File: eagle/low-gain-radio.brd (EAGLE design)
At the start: 99 x 100 mm, 109 parts, among them Y1 32MHz

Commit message: Added to-do lists
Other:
- board text added: "TODO: -Add PSAS and people who helped with board text -Figure out footprint drc error -I'm guessing we are ignoring the dimension drc error on the MCX???"
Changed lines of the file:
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@@
 <layer number="98" name="Guide" color="6" fill="1" visible="no" active="no"/>
 <layer number="99" name="SpiceOrder" color="7" fill="1" visible="no" active="no"/>
-<layer number="100" name="TODO" color="12" fill="1" visible="no" active="yes"/>
+<layer number="100" name="TODO" color="12" fill="1" visible="yes" active="yes"/>
 <layer number="101" name="Hidden" color="7" fill="1" visible="no" active="yes"/>
 <layer number="102" name="Changes" color="7" fill="1" visible="no" active="yes"/>
@@
 <text x="55.2" y="53.05" size="1" layer="21" font="vector" ratio="16" rot="R180">DIO4</text>
 <text x="45.05" y="86.5" size="1" layer="21" font="vector" ratio="16">PG</text>
+<text x="65.45" y="30.4" size="0.4064" layer="100">TODO:
+-Add PSAS and people who helped with board text
+-Figure out footprint drc error
+-I'm guessing we are ignoring the dimension drc error on the MCX???</text>
 </plain>
 <attributes>

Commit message: Pushing for Andrew
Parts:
- CF2: value CON-MCX-LINX -> CON-MCX-F-LINX-CONMCX003.062
- moved CF2 2.86 mm to (72.0, 93.0)
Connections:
- removed net ASD: C47.1
- net RF_GND: now also C47.1, CF2.SHIELD1, CF2.SHIELD2, CF2.SHIELD3, CF2.SHIELD4
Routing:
- net N$30: track 3.79 -> 9.46 mm
- net RF_GND: track 11.8 -> 13.7 mm
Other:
- outline, holes or cut-outs redrawn
- board text added: "TODO: -Add PSAS and people who helped with board text -Via stitching"
- board text removed: "Cut power plane to here"
- board text removed: "TODO: -Add PSAS and people who helped with board text -Figure out footprint drc error -I'm guessing we are ignoring the dimension drc error on the MCX???"
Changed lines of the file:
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@@
 <text x="35" y="0.6" size="1" layer="21" font="vector" ratio="16">C2</text>
 <text x="14.2" y="0.6" size="1" layer="21" font="vector" ratio="16">GND</text>
-<wire x1="49.8" y1="89.6" x2="49.85" y2="89.6" width="0.2" layer="100" style="longdash"/>
-<wire x1="49.85" y1="89.6" x2="49.85" y2="71.25" width="0.2" layer="100" style="shortdash"/>
-<wire x1="49.85" y1="71.25" x2="59.75" y2="71.25" width="0.2" layer="100" style="shortdash"/>
-<text x="49.65" y="90.35" size="0.75" layer="100">Cut power plane to here</text>
 <text x="62.15" y="62.8" size="1" layer="21" font="vector" ratio="16">XTA</text>
 <text x="97.45" y="71.6" size="1" layer="21" font="vector" ratio="16" rot="R180">SCLK</text>
@@
 <text x="65.45" y="30.4" size="0.4064" layer="100">TODO:
 -Add PSAS and people who helped with board text
--Figure out footprint drc error
--I'm guessing we are ignoring the dimension drc error on the MCX???</text>
+-Via stitching</text>
 </plain>
 <attributes>
@@
 </element>
 <element name="CF1" library="oresat-eagle" package="HARWIN-ARCHER-M50-3202045" value="ORESAT-CONNECTOR-40PIN" x="30.065" y="95.46" locked="yes" rot="R180"/>
-<element name="CF2" library="oresat-eagle" package="CON-MCX-LINX-CONMCX003.062" value="CON-MCX-LINX" x="72.04" y="90.119" locked="yes" rot="R90"/>
+<element name="CF2" library="oresat-eagle" package="CON-MCX-LINX-CONMCX003.062" value="CON-MCX-F-LINX-CONMCX003.062" x="72.04" y="92.9784" rot="R90"/>
 <element name="U$35" library="oresat-eagle" package="ORESAT-CARD-RF-V0.3" value="" x="0" y="0" locked="yes"/>
 <element name="TP18" library="testpad" package="P1-13" value="TPSPAD1-13" x="63.317915625" y="61.437253125">
@@
 <contactref element="TRSWITCH" pad="5"/>
 <contactref element="CF2" pad="CENTER"/>
-<wire x1="72" y1="88.404" x2="72.04" y2="88.404" width="0.2" layer="1"/>
+<wire x1="72" y1="88.404" x2="72.04" y2="91.2634" width="0.2" layer="1"/>
 <wire x1="72.016" y1="84.664" x2="72.02" y2="84.664" width="0.2" layer="1"/>
 <wire x1="72.02" y1="84.664" x2="72.02" y2="85.1" width="0.2" layer="1"/>
 <wire x1="72.02" y1="85.1" x2="72.02" y2="88.384" width="0.343" layer="1"/>
-<wire x1="72.02" y1="88.384" x2="72.04" y2="88.404" width="0.343" layer="1"/>
+<wire x1="72.02" y1="88.384" x2="72.04" y2="91.2634" width="0.343" layer="1"/>
 </signal>
 <signal name="VR_PA">
@@
 <via x="42.13" y="64.92" extent="1-16" drill="0.254"/>
 <wire x1="42.13" y1="98" x2="42.13" y2="96.85" width="0.2" layer="16"/>
-<wire x1="42.13" y1="96.85" x2="45.95" y2="96.85" width="0.2" layer="16"/>
-<wire x1="45.95" y1="96.85" x2="45.95" y2="88.9" width="0.2" layer="16"/>
+<wire x1="42.13" y1="96.85" x2="45.75" y2="96.85" width="0.2" layer="16"/>
+<wire x1="45.75" y1="96.85" x2="45.75" y2="88.9" width="0.2" layer="16"/>
 <wire x1="42.13" y1="64.92" x2="42.13" y2="88.9" width="0.2" layer="16"/>
-<wire x1="42.13" y1="88.9" x2="45.95" y2="88.9" width="0.2" layer="16"/>
+<wire x1="42.13" y1="88.9" x2="45.75" y2="88.9" width="0.2" layer="16"/>
 </signal>
 <signal name="PTB17">
@@
 <wire x1="38.29" y1="0.67" x2="38.29" y2="3.6" width="0.2" layer="16"/>
 <wire x1="40.86" y1="98" x2="40.86" y2="96.4" width="0.2" layer="16"/>
-<wire x1="40.86" y1="96.4" x2="45.55" y2="96.4" width="0.2" layer="16"/>
-<wire x1="45.55" y1="96.4" x2="45.55" y2="89.3" width="0.2" layer="16"/>
-<wire x1="45.55" y1="89.3" x2="40.85" y2="89.3" width="0.2" layer="16"/>
+<wire x1="40.86" y1="96.4" x2="45.35" y2="96.4" width="0.2" layer="16"/>
+<wire x1="45.35" y1="96.4" x2="45.35" y2="89.3" width="0.2" layer="16"/>
+<wire x1="45.35" y1="89.3" x2="40.85" y2="89.3" width="0.2" layer="16"/>
 <wire x1="40.85" y1="89.3" x2="40.85" y2="11.58" width="0.2" layer="16"/>
 <wire x1="40.85" y1="11.58" x2="40.82" y2="11.58" width="0.2" layer="16"/>
@@
 <wire x1="33.21" y1="41.04" x2="35.13" y2="41.04" width="0.2" layer="16"/>
 <wire x1="39.59" y1="98" x2="39.59" y2="96" width="0.2" layer="16"/>
-<wire x1="39.59" y1="96" x2="45.05" y2="96" width="0.2" layer="16"/>
-<wire x1="45.05" y1="96" x2="45.05" y2="89.7" width="0.2" layer="16"/>
-<wire x1="45.05" y1="89.7" x2="39.6" y2="89.7" width="0.2" layer="16"/>
+<wire x1="39.59" y1="96" x2="44.95" y2="96" width="0.2" layer="16"/>
+<wire x1="44.95" y1="96" x2="44.95" y2="89.7" width="0.2" layer="16"/>
+<wire x1="44.95" y1="89.7" x2="39.6" y2="89.7" width="0.2" layer="16"/>
 <wire x1="39.6" y1="89.7" x2="39.6" y2="55.2" width="0.2" layer="16"/>
 </signal>
@@
 <contactref element="R12" pad="1"/>
 <wire x1="83.4" y1="6.2" x2="83.4" y2="4.65" width="0.2" layer="1"/>
-</signal>
-<signal name="ASD">
-<contactref element="C47" pad="1"/>
 </signal>
 <signal name="N$2">
@@
 <wire x1="76.05" y1="64.4" x2="76.05" y2="63.9" width="0.2" layer="1"/>
 <wire x1="76.05" y1="63.9" x2="75.9" y2="63.75" width="0.2" layer="1"/>
-<wire x1="58.3" y1="87.6" x2="58.9" y2="88.95" width="0" layer="19" extent="1-1"/>
+<wire x1="58.3" y1="87.6" x2="58.9" y2="87.6" width="0.4064" layer="1"/>
+<wire x1="58.9" y1="88.95" x2="58.9" y2="87.6" width="0.4064" layer="1"/>
+<contactref element="CF2" pad="SHIELD3"/>
+<contactref element="CF2" pad="SHIELD2"/>
+<contactref element="CF2" pad="SHIELD4"/>
+<contactref element="CF2" pad="SHIELD1"/>
+<contactref element="C47" pad="1"/>
+<wire x1="93.35" y1="80.7" x2="94.65" y2="80.2" width="0" layer="19" extent="1-1"/>
+<wire x1="74.78" y1="91.2634" x2="74.78" y2="91.2634" width="0" layer="19" extent="1-16"/>
+<wire x1="69.3" y1="91.2634" x2="69.3" y2="91.2634" width="0" layer="19" extent="1-16"/>
 </signal>
 </signals>

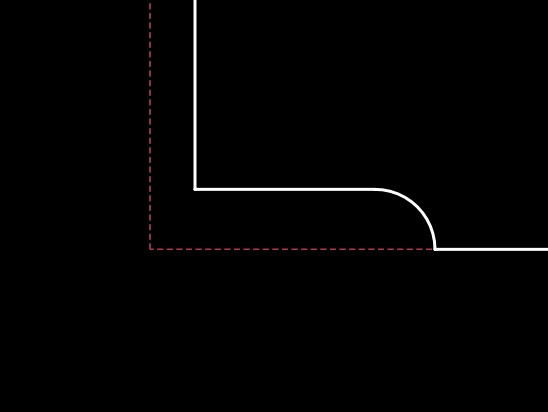
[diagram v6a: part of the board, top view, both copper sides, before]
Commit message: Fixed RF_GND/GND warnings by creating new RF_GND symbol in oresat-eagle-libraries. Added bypass cap on TX/RX inverter.
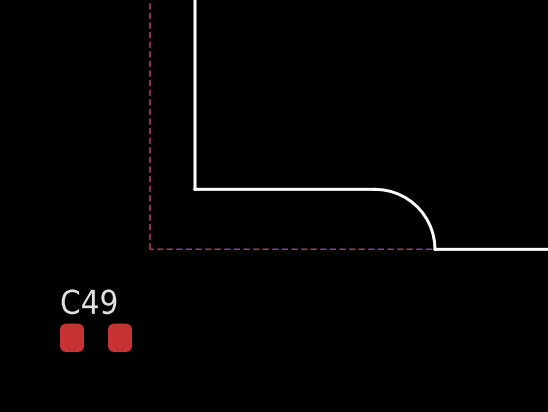
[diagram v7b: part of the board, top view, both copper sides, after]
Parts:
- added C49: 100nF, rcl_custom:.0603-B-NOSILK
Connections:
- net GND: no longer C36.1, C37.1, C38.1, C48.1, U$7.2
- net RF_GND: now also C36.1, C37.1, C38.1, C48.1, C49.1, U$7.2
- net V+: now also C49.2

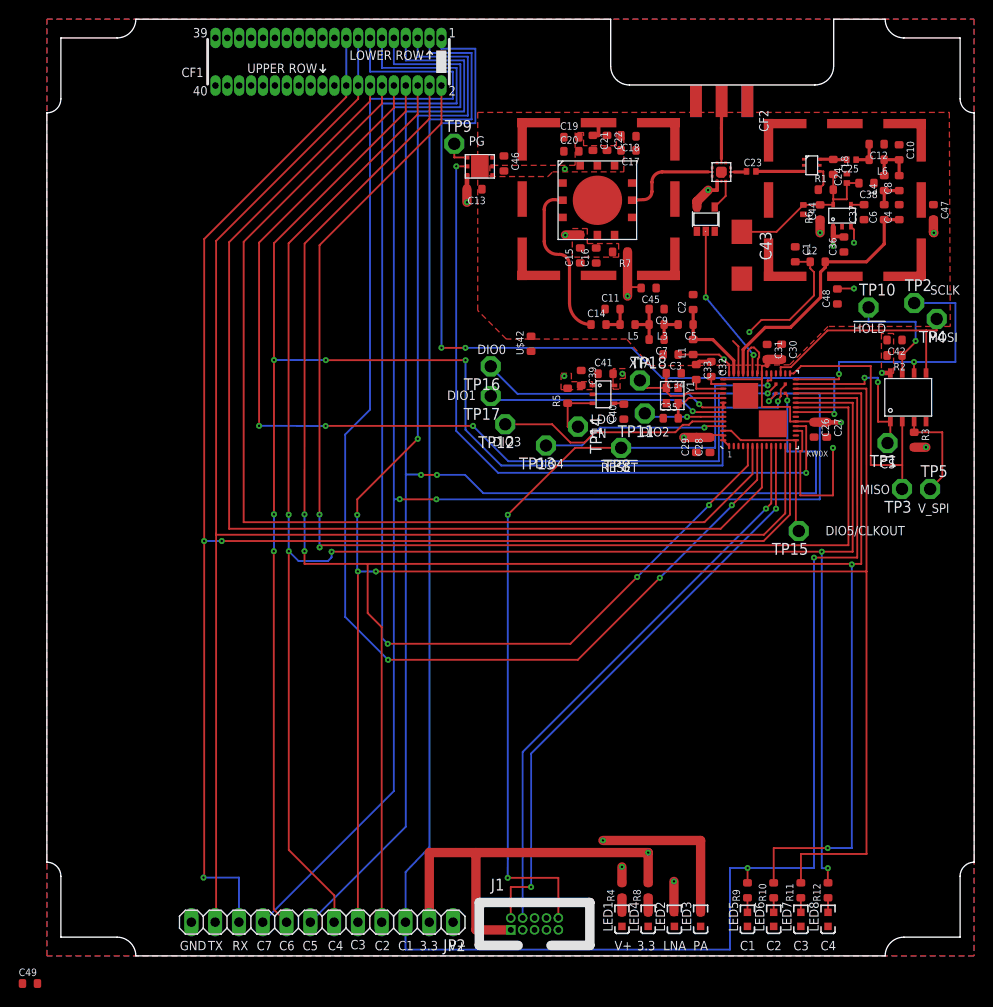
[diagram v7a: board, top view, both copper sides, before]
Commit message: Added bypass cap and PSAS text to the board
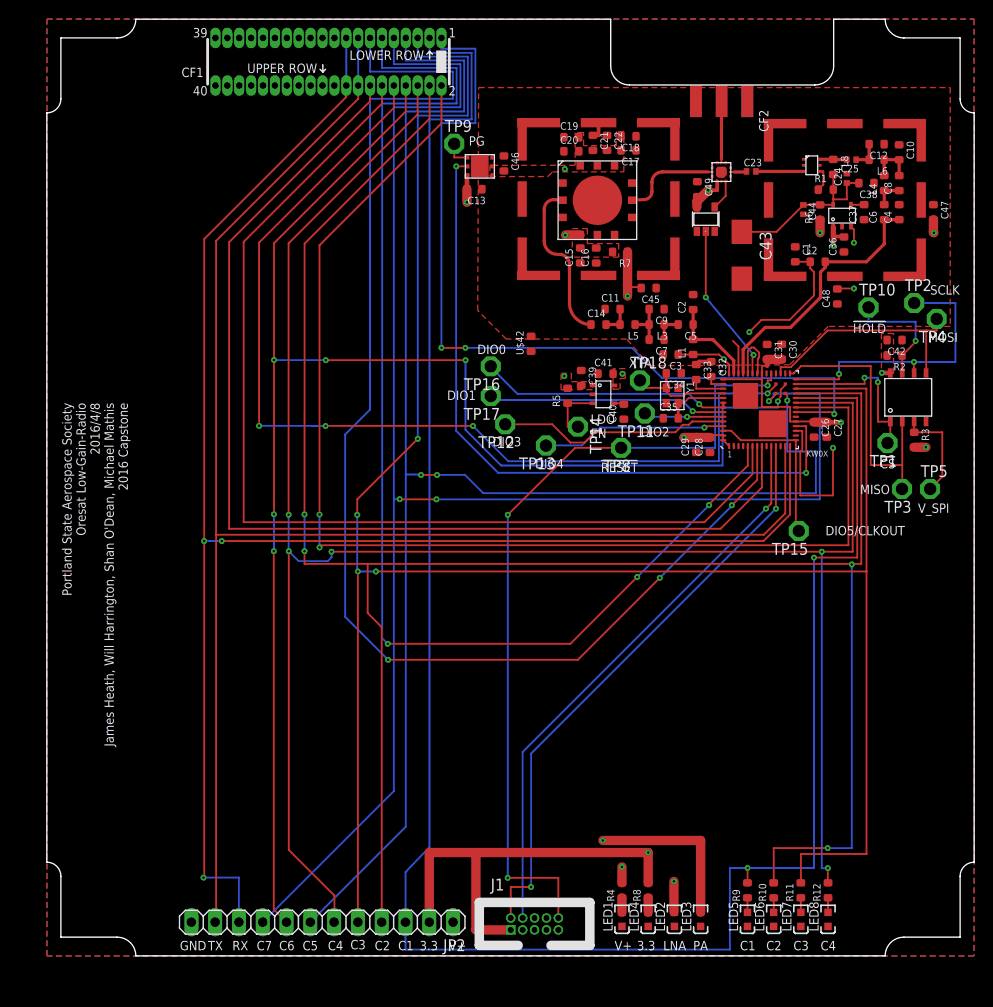
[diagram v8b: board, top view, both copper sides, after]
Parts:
- moved C49 110.8 mm to (69.5, 81.8), turned to 270 degrees
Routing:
- net V+: track 127.6 -> 128.2 mm
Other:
- board text added: "Portland State Aerospace Society Oresat Low-Gain-Radio 2016/4/8 James Heath, Will Harrington, Shan O'Dean, Michael Mathis 2016 Capstone"
- board text added: "TODO: -Via stitching"
- board text removed: "TODO: -Add PSAS and people who helped with board text -Via stitching"
